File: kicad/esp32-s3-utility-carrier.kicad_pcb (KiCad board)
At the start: 2 copper layers, 130 x 85 mm, 25 parts, among them U2 SN74AHCT125N

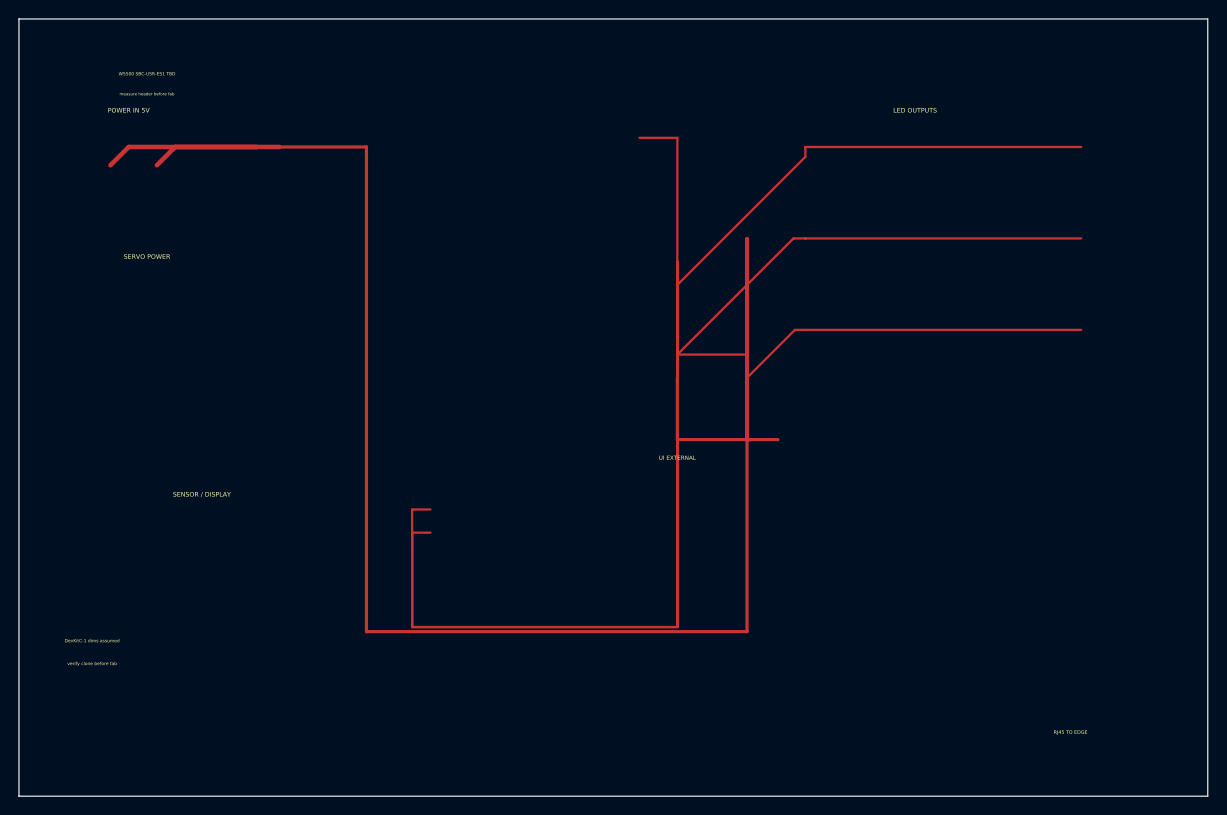
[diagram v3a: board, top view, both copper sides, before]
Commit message: fix(pcb): connect minimal carrier power and LED nets
Co-authored-by: Cursor <cursoragent@cursor.com>
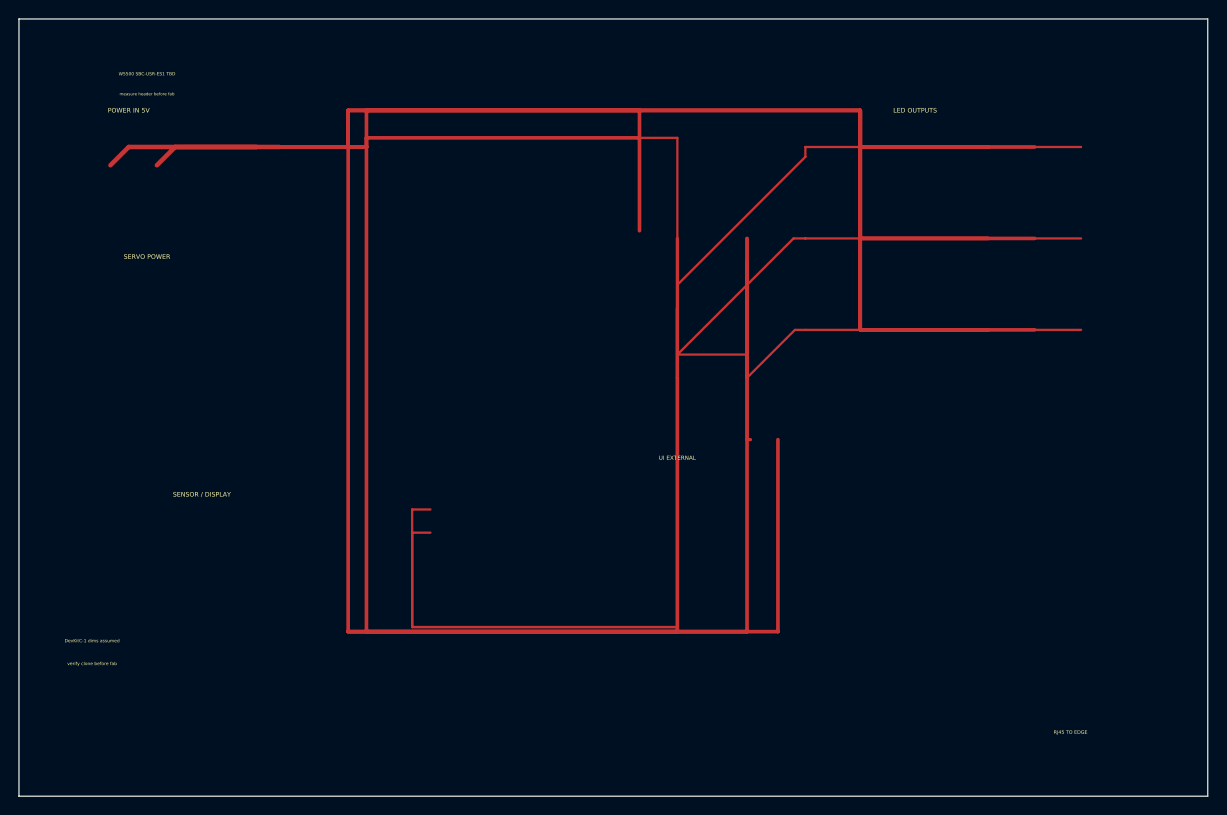
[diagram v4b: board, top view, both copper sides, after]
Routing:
- net GND: track 32.0 -> 455.4 mm
- net 5V_LED: track 0.00 -> 154.0 mm
- net 5V_LOGIC: track 172.0 -> 214.9 mm
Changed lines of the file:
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@@
   (segment (start 15.08 16) (end 17.08 14.0) (width 0.5) (layer "F.Cu") (net 2))
   (segment (start 17.08 14.0) (end 28.5 14) (width 0.5) (layer "F.Cu") (net 2))
-  (segment (start 26 14) (end 38.0 14) (width 0.35) (layer "F.Cu") (net 3))
-  (segment (start 38.0 14) (end 38.0 67.0) (width 0.35) (layer "F.Cu") (net 3))
-  (segment (start 38.0 67.0) (end 79.62 67.0) (width 0.35) (layer "F.Cu") (net 3))
-  (segment (start 79.62 67.0) (end 79.62 24) (width 0.35) (layer "F.Cu") (net 3))
+  (segment (start 26 14) (end 38.0 14) (width 0.4) (layer "F.Cu") (net 3))
+  (segment (start 38.0 14) (end 38.0 67.0) (width 0.4) (layer "F.Cu") (net 3))
+  (segment (start 38.0 67.0) (end 79.62 67.0) (width 0.4) (layer "F.Cu") (net 3))
+  (segment (start 79.62 67.0) (end 79.62 24) (width 0.4) (layer "F.Cu") (net 3))
+  (segment (start 26 14) (end 38.0 14) (width 0.4) (layer "F.Cu") (net 3))
+  (segment (start 38.0 14) (end 38.0 13.0) (width 0.4) (layer "F.Cu") (net 3))
+  (segment (start 38.0 13.0) (end 67.86 13.0) (width 0.4) (layer "F.Cu") (net 3))
   (segment (start 79.62 24) (end 79.62 46) (width 0.35) (layer "F.Cu") (net 3))
   (segment (start 79.62 46) (end 80 46) (width 0.35) (layer "F.Cu") (net 3))
-  (segment (start 72 39.24) (end 72 46) (width 0.35) (layer "F.Cu") (net 2))
-  (segment (start 72 46) (end 83.0 46) (width 0.35) (layer "F.Cu") (net 2))
+  (segment (start 28.5 14) (end 36.0 14) (width 0.4) (layer "F.Cu") (net 2))
+  (segment (start 36.0 14) (end 36.0 10.0) (width 0.4) (layer "F.Cu") (net 2))
+  (segment (start 67.86 23.16) (end 67.86 10.0) (width 0.4) (layer "F.Cu") (net 2))
+  (segment (start 67.86 10.0) (end 36.0 10.0) (width 0.4) (layer "F.Cu") (net 2))
+  (segment (start 72 39.24) (end 72 67.0) (width 0.4) (layer "F.Cu") (net 2))
+  (segment (start 72 67.0) (end 36.0 67.0) (width 0.4) (layer "F.Cu") (net 2))
+  (segment (start 36.0 67.0) (end 36.0 10.0) (width 0.4) (layer "F.Cu") (net 2))
+  (segment (start 83.0 46) (end 83.0 67.0) (width 0.4) (layer "F.Cu") (net 2))
+  (segment (start 83.0 67.0) (end 36.0 67.0) (width 0.4) (layer "F.Cu") (net 2))
+  (segment (start 72 24) (end 72 39.24) (width 0.35) (layer "F.Cu") (net 2))
+  (segment (start 72 31.62) (end 72 39.24) (width 0.35) (layer "F.Cu") (net 2))
+  (segment (start 79.62 34.16) (end 79.62 39.24) (width 0.35) (layer "F.Cu") (net 2))
+  (segment (start 79.62 26.54) (end 79.62 39.24) (width 0.35) (layer "F.Cu") (net 2))
+  (segment (start 26 14) (end 38.0 14) (width 0.4) (layer "F.Cu") (net 4))
+  (segment (start 38.0 14) (end 38.0 10.0) (width 0.4) (layer "F.Cu") (net 4))
+  (segment (start 38.0 10.0) (end 92.0 10.0) (width 0.4) (layer "F.Cu") (net 4))
+  (segment (start 36.0 10.0) (end 92.0 10.0) (width 0.4) (layer "F.Cu") (net 2))
+  (segment (start 92.0 10.0) (end 92.0 14) (width 0.4) (layer "F.Cu") (net 4))
+  (segment (start 92.0 14) (end 106 14) (width 0.4) (layer "F.Cu") (net 4))
+  (segment (start 92.0 10.0) (end 92.0 14) (width 0.4) (layer "F.Cu") (net 2))
+  (segment (start 92.0 14) (end 111.08 14) (width 0.4) (layer "F.Cu") (net 2))
+  (segment (start 92.0 10.0) (end 92.0 24) (width 0.4) (layer "F.Cu") (net 4))
+  (segment (start 92.0 24) (end 106 24) (width 0.4) (layer "F.Cu") (net 4))
+  (segment (start 92.0 10.0) (end 92.0 24) (width 0.4) (layer "F.Cu") (net 2))
+  (segment (start 92.0 24) (end 111.08 24) (width 0.4) (layer "F.Cu") (net 2))
+  (segment (start 92.0 10.0) (end 92.0 34) (width 0.4) (layer "F.Cu") (net 4))
+  (segment (start 92.0 34) (end 106 34) (width 0.4) (layer "F.Cu") (net 4))
+  (segment (start 92.0 10.0) (end 92.0 34) (width 0.4) (layer "F.Cu") (net 2))
+  (segment (start 92.0 34) (end 111.08 34) (width 0.4) (layer "F.Cu") (net 2))
 )
